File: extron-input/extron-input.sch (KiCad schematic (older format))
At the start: 16 parts, among them J1 SCART-F, J10 Conn_01x01, J11 Conn_01x01, J2 RED, J3 GREEN, J4 BLUE, J5 SYNC, J6 PHOENIX, J7 SENSE, J8 Conn_01x01, J9 Conn_01x01, SW1 SW_DPDT_x2, U1 LM1881

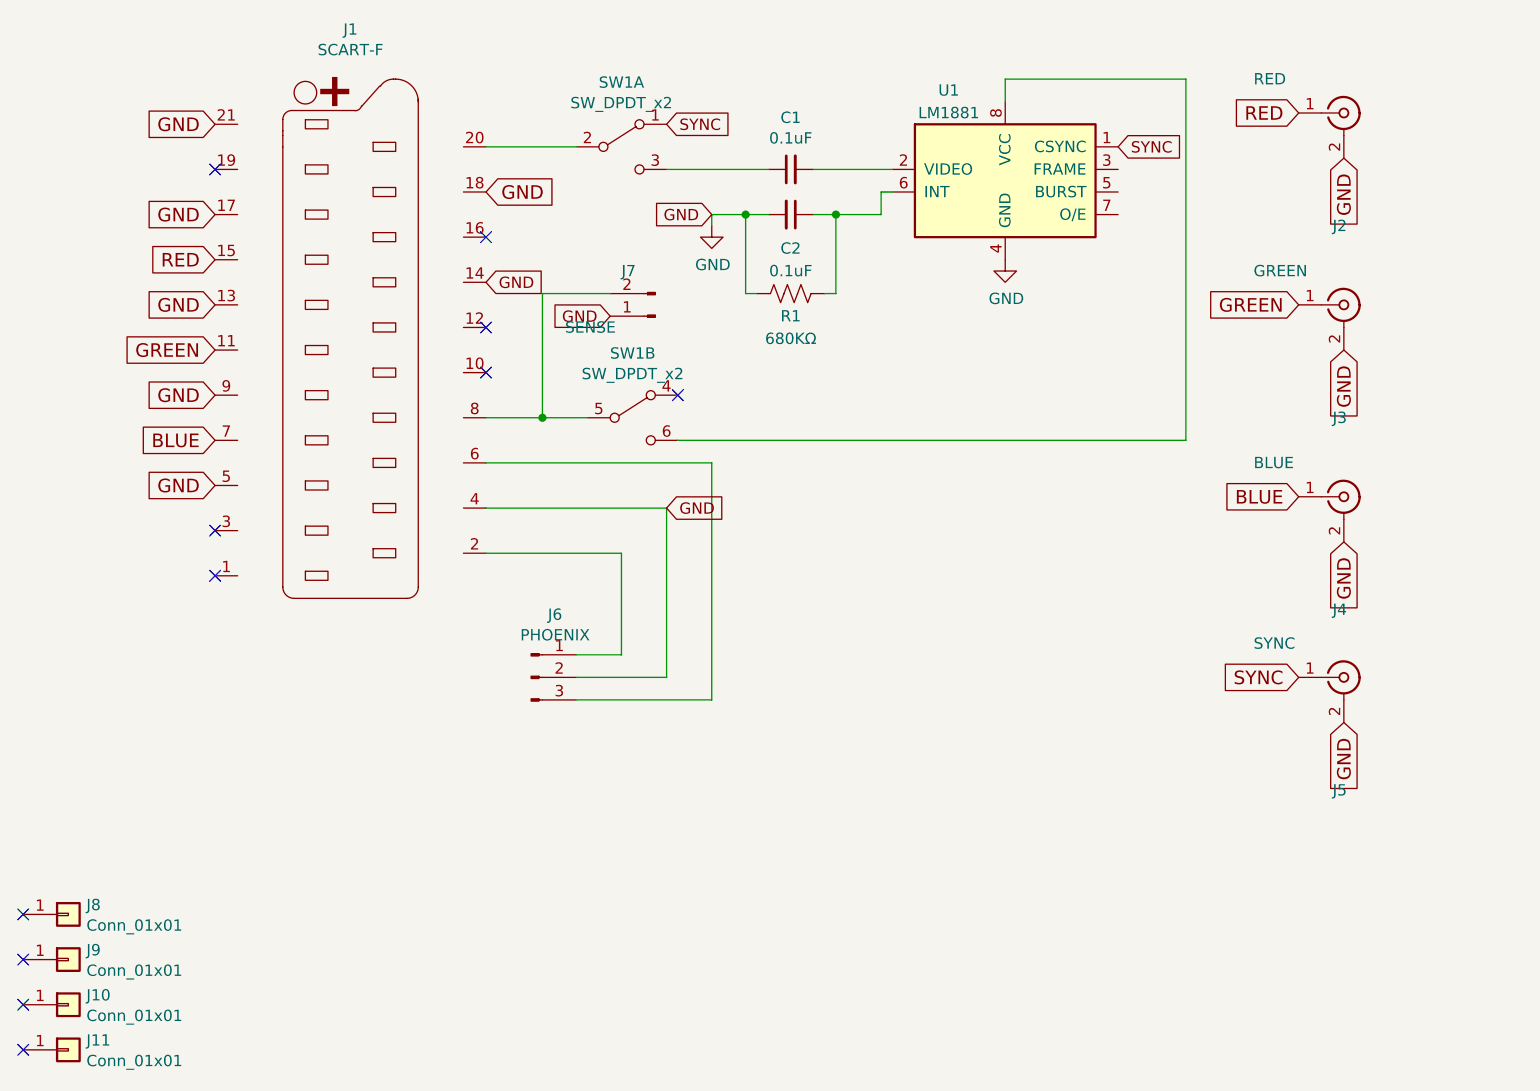
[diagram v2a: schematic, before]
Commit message: Rev 2 input board (+ other small things)
BNC F -> RCA F for all outputs to extron
  The BNC is great, but expensive, and also impossible to close over an
  extron input when they are matrixed. The RCA female recepticles will
  all to use with RCA M -> BNC M adapters, which you can pre-load onto
  the extron BNC F inputs. This will allow cards to plug in
  individually, or all at once if you have a stack of cards held
  together with standoffs.

Sense circuit protection
  Added to the input board to create a 3v3 sense line to be used by an
  upcoming optional board. It also protects the SCART switch line from
  output from the optional board, just in case. This entire circuit is
  totally optional. If you're not using the upcoming sense board, then
  you can leave this unpopulated.

New footprints for 2 different types of RCA
  There's an available RCA female PCB mount footprint that I found here:
  http://smisioto.no-ip.org/elettronica/kicad/kicad-en.htm . I also
  created my own footprint for the only RCA part on lcsc.com, because if
  that one works, it's super inexpensive. You can use one or the other,
  I hope.

Gitignore added
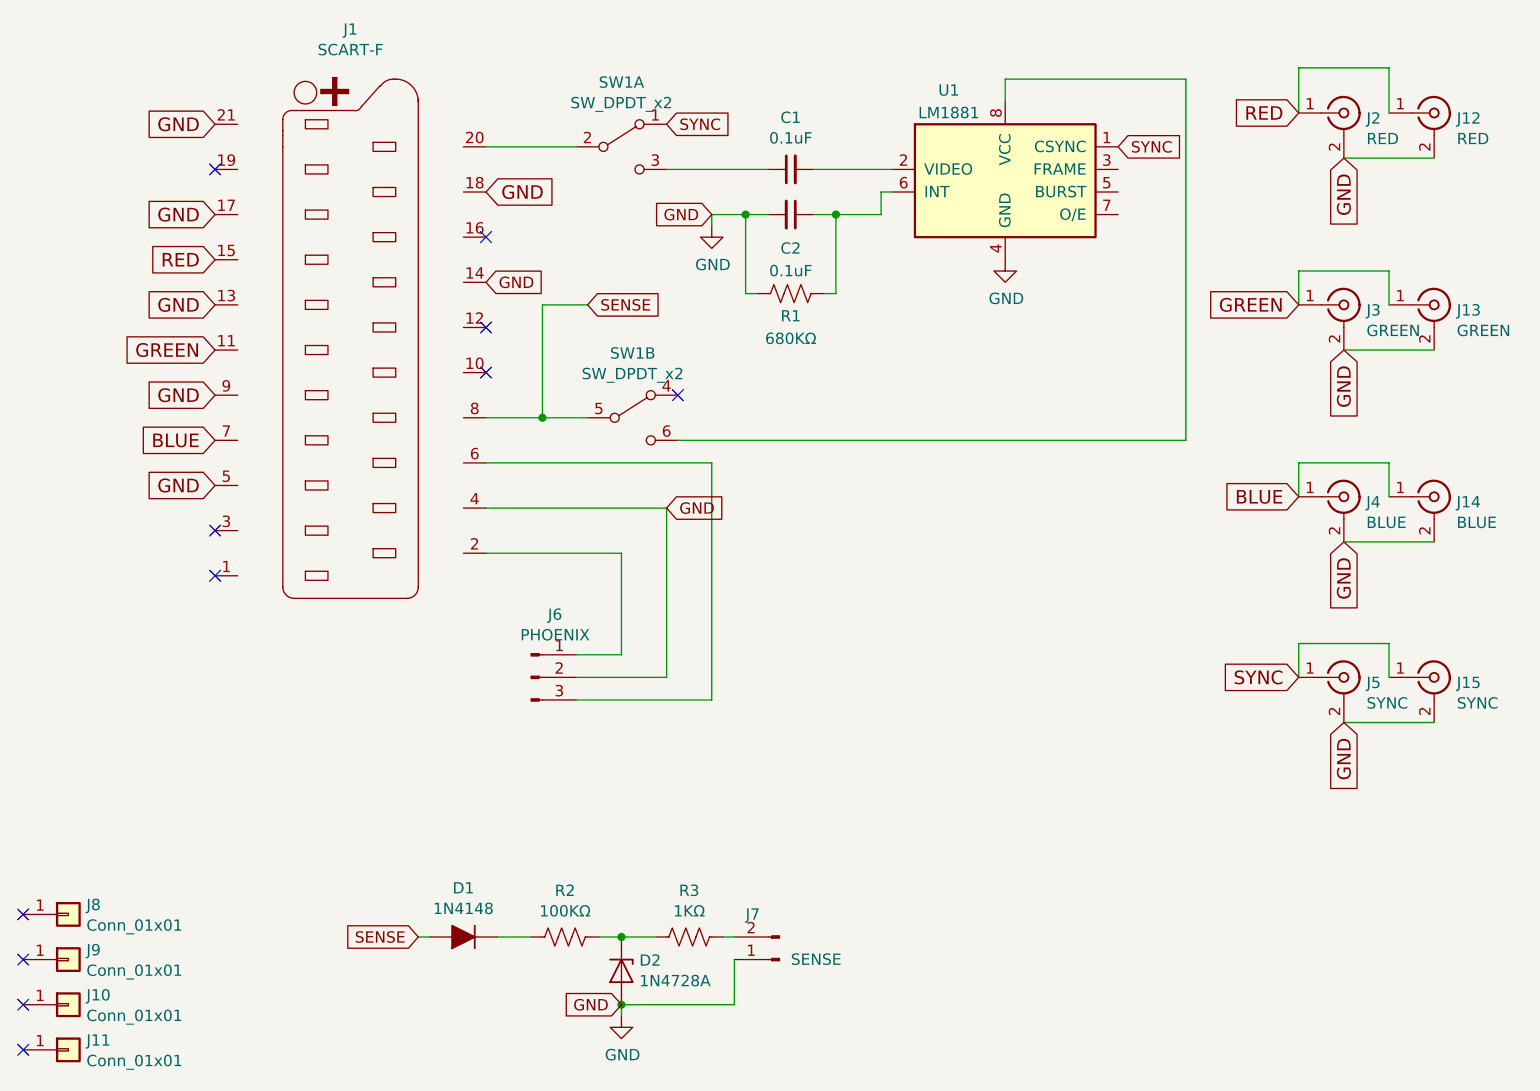
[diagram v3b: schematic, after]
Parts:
- added D1: 1N4148, Diode_THT:D_DO-35_SOD27_P2.54mm_Vertical_AnodeUp, symbol Device:D_ALT
- added D2: 1N4728A, Diode_THT:D_DO-35_SOD27_P2.54mm_Vertical_AnodeUp, symbol Device:D_Zener
- added J12: RED, extron-input:rca_black, symbol Connector:Conn_Coaxial
- added J13: GREEN, extron-input:rca_black, symbol Connector:Conn_Coaxial
- added J14: BLUE, extron-input:rca_black, symbol Connector:Conn_Coaxial
- added J15: SYNC, extron-input:rca_black, symbol Connector:Conn_Coaxial
- added R2: 100KΩ, Resistor_THT:R_Axial_DIN0204_L3.6mm_D1.6mm_P1.90mm_Vertical, symbol Device:R_US
- added R3: 1KΩ, Resistor_THT:R_Axial_DIN0204_L3.6mm_D1.6mm_P1.90mm_Vertical, symbol Device:R_US
- J2, J3, J4, J5: footprint extron-input:BNC_90 -> extron-input:rca_boom
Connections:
- net BLUE: now also J14.1 (In)
- net GND: now also D2.2 (A), J12.2 (Ext), J13.2 (Ext), J14.2 (Ext), J15.2 (Ext)
- net GREEN: now also J13.1 (In)
- net RED: now also J12.1 (In)
- net SYNC: now also J15.1 (In)
- net SENSE: now reaches J1.8 (P8), SW1.5 (B)
- net SENSE: now also D1.2 (A); no longer J7.2 (Pin_2)
- new net: J7.2 (Pin_2), R3.1
- new net: D1.1 (K), R2.2
- new net: D2.1 (K), R2.1, R3.2
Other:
- moved on the sheet: J7
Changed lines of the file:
@@
 Text GLabel 8050 2050 0    60   Input ~ 0
 RED
-$Comp
-L Connector:Conn_Coaxial J2
-U 1 1 5C651C5B
-P 8250 2050
-F 0 "J2" H 8200 1550 50  0000 L CNN
-F 1 "RED" H 7850 2200 50  0000 L CNN
-F 2 "extron-input:BNC_90" H 8250 2050 50  0001 C CNN
-F 3 " ~" H 8250 2050 50  0001 C CNN
-	1    8250 2050
-	1    0    0    -1
-$EndComp
-$Comp
-L Connector:Conn_Coaxial J3
-U 1 1 5C651D00
-P 8250 2900
-F 0 "J3" H 8200 2400 50  0000 L CNN
-F 1 "GREEN" H 7850 3050 50  0000 L CNN
-F 2 "extron-input:BNC_90" H 8250 2900 50  0001 C CNN
-F 3 " ~" H 8250 2900 50  0001 C CNN
-	1    8250 2900
-	1    0    0    -1
-$EndComp
-$Comp
-L Connector:Conn_Coaxial J4
-U 1 1 5C651DB2
-P 8250 3750
-F 0 "J4" H 8200 3250 50  0000 L CNN
-F 1 "BLUE" H 7850 3900 50  0000 L CNN
-F 2 "extron-input:BNC_90" H 8250 3750 50  0001 C CNN
-F 3 " ~" H 8250 3750 50  0001 C CNN
-	1    8250 3750
-	1    0    0    -1
-$EndComp
-$Comp
-L Connector:Conn_Coaxial J5
-U 1 1 5C651E83
-P 8250 4550
-F 0 "J5" H 8200 4050 50  0000 L CNN
-F 1 "SYNC" H 7850 4700 50  0000 L CNN
-F 2 "extron-input:BNC_90" H 8250 4550 50  0001 C CNN
-F 3 " ~" H 8250 4550 50  0001 C CNN
-	1    8250 4550
-	1    0    0    -1
-$EndComp
 Text GLabel 8250 3100 3    60   Input ~ 0
 GND
@@
 L Connector:Conn_01x02_Male J7
 U 1 1 5C74DAFA
-P 5200 2950
-F 0 "J7" H 5350 2750 50  0000 R CNN
-F 1 "SENSE" H 5600 3000 50  0000 R CNN
-F 2 "Connector_JST:JST_XH_S02B-XH-A_1x02_P2.50mm_Horizontal" H 5200 2950 50  0001 C CNN
-F 3 "~" H 5200 2950 50  0001 C CNN
-	1    5200 2950
+P 5750 5800
+F 0 "J7" H 5900 5600 50  0000 R CNN
+F 1 "SENSE" H 5700 5800 50  0000 R CNN
+F 2 "Connector_JST:JST_XH_S02B-XH-A_1x02_P2.50mm_Horizontal" H 5750 5800 50  0001 C CNN
+F 3 "~" H 5750 5800 50  0001 C CNN
+	1    5750 5800
 	-1   0    0    1
 $EndComp
@@
 Wire Wire Line
 	4700 3400 4900 3400
-Text GLabel 5000 2950 0    50   Input ~ 0
+Text GLabel 5050 6000 0    50   Input ~ 0
 GND
 Wire Wire Line
@@
 	4850 4650 5450 4650
 Wire Wire Line
-	4700 2850 5000 2850
-Wire Wire Line
-	4700 2850 4700 3400
+	4700 2900 4900 2900
+Wire Wire Line
+	4700 2900 4700 3400
+Text GLabel 4900 2900 2    50   Input ~ 0
+SENSE
+Wire Wire Line
+	5550 5700 5500 5700
+$Comp
+L Device:D_ALT D1
+U 1 1 5C84733C
+P 4350 5700
+F 0 "D1" H 4350 5484 50  0000 C CNN
+F 1 "1N4148" H 4350 5575 50  0000 C CNN
+F 2 "Diode_THT:D_DO-35_SOD27_P2.54mm_Vertical_AnodeUp" H 4350 5700 50  0001 C CNN
+F 3 "~" H 4350 5700 50  0001 C CNN
+	1    4350 5700
+	-1   0    0    1
+$EndComp
+$Comp
+L Device:R_US R2
+U 1 1 5C847B71
+P 4800 5700
+F 0 "R2" V 4595 5700 50  0000 C CNN
+F 1 "100KΩ" V 4686 5700 50  0000 C CNN
+F 2 "Resistor_THT:R_Axial_DIN0204_L3.6mm_D1.6mm_P1.90mm_Vertical" V 4840 5690 50  0001 C CNN
+F 3 "~" H 4800 5700 50  0001 C CNN
+	1    4800 5700
+	0    1    1    0
+$EndComp
+$Comp
+L Device:D_Zener D2
+U 1 1 5C847C9D
+P 5050 5850
+F 0 "D2" V 5004 5929 50  0000 L CNN
+F 1 "1N4728A" V 5095 5929 50  0000 L CNN
+F 2 "Diode_THT:D_DO-35_SOD27_P2.54mm_Vertical_AnodeUp" H 5050 5850 50  0001 C CNN
+F 3 "~" H 5050 5850 50  0001 C CNN
+	1    5050 5850
+	0    1    1    0
+$EndComp
+Wire Wire Line
+	4950 5700 5050 5700
+Connection ~ 5050 5700
+Text GLabel 4150 5700 0    50   Input ~ 0
+SENSE
+$Comp
+L power:GND #PWR0103
+U 1 1 5C849937
+P 5050 6050
+F 0 "#PWR0103" H 5050 5800 50  0001 C CNN
+F 1 "GND" H 5055 5877 50  0000 C CNN
+F 2 "" H 5050 6050 50  0001 C CNN
+F 3 "" H 5050 6050 50  0001 C CNN
+	1    5050 6050
+	1    0    0    -1
+$EndComp
+Wire Wire Line
+	5550 5800 5550 6000
+Wire Wire Line
+	5550 6000 5050 6000
+Connection ~ 5050 6000
+Wire Wire Line
+	5050 6000 5050 6050
+$Comp
+L Device:R_US R3
+U 1 1 5C84AF3E
+P 5350 5700
+F 0 "R3" V 5145 5700 50  0000 C CNN
+F 1 "1KΩ" V 5236 5700 50  0000 C CNN
+F 2 "Resistor_THT:R_Axial_DIN0204_L3.6mm_D1.6mm_P1.90mm_Vertical" V 5390 5690 50  0001 C CNN
+F 3 "~" H 5350 5700 50  0001 C CNN
+	1    5350 5700
+	0    1    1    0
+$EndComp
+Wire Wire Line
+	5200 5700 5050 5700
+Wire Wire Line
+	4150 5700 4200 5700
+Wire Wire Line
+	4500 5700 4650 5700
+$Comp
+L Connector:Conn_Coaxial J12
+U 1 1 5C84CB4A
+P 8650 2050
+F 0 "J12" H 8750 2026 50  0000 L CNN
+F 1 "RED" H 8750 1935 50  0000 L CNN
+F 2 "extron-input:rca_black" H 8650 2050 50  0001 C CNN
+F 3 " ~" H 8650 2050 50  0001 C CNN
+	1    8650 2050
+	1    0    0    -1
+$EndComp
+Wire Wire Line
+	8050 1850 8050 2050
+Wire Wire Line
+	8250 2250 8650 2250
+Wire Wire Line
+	8050 1850 8450 1850
+Wire Wire Line
+	8450 1850 8450 2050
+$Comp
+L Connector:Conn_Coaxial J13
+U 1 1 5C84FDFD
+P 8650 2900
+F 0 "J13" H 8750 2876 50  0000 L CNN
+F 1 "GREEN" H 8750 2785 50  0000 L CNN
+F 2 "extron-input:rca_black" H 8650 2900 50  0001 C CNN
+F 3 " ~" H 8650 2900 50  0001 C CNN
+	1    8650 2900
+	1    0    0    -1
+$EndComp
+$Comp
+L Connector:Conn_Coaxial J14
+U 1 1 5C84FE72
+P 8650 3750
+F 0 "J14" H 8749 3726 50  0000 L CNN
+F 1 "BLUE" H 8749 3635 50  0000 L CNN
+F 2 "extron-input:rca_black" H 8650 3750 50  0001 C CNN
+F 3 " ~" H 8650 3750 50  0001 C CNN
+	1    8650 3750
+	1    0    0    -1
+$EndComp
+$Comp
+L Connector:Conn_Coaxial J15
+U 1 1 5C84FF62
+P 8650 4550
+F 0 "J15" H 8750 4526 50  0000 L CNN
+F 1 "SYNC" H 8750 4435 50  0000 L CNN
+F 2 "extron-input:rca_black" H 8650 4550 50  0001 C CNN
+F 3 " ~" H 8650 4550 50  0001 C CNN
+	1    8650 4550
+	1    0    0    -1
+$EndComp
+Wire Wire Line
+	8650 4750 8250 4750
+Wire Wire Line
+	8450 4550 8450 4400
+Wire Wire Line
+	8450 4400 8050 4400
+Wire Wire Line
+	8050 4400 8050 4550
+Wire Wire Line
+	8650 3950 8250 3950
+Wire Wire Line
+	8050 3750 8050 3600
+Wire Wire Line
+	8050 3600 8450 3600
+Wire Wire Line
+	8450 3600 8450 3750
+Wire Wire Line
+	8250 3100 8650 3100
+Wire Wire Line
+	8050 2900 8050 2750
+Wire Wire Line
+	8050 2750 8450 2750
+Wire Wire Line
+	8450 2750 8450 2900
+$Comp
+L Connector:Conn_Coaxial J2
+U 1 1 5C8498CA
+P 8250 2050
+F 0 "J2" H 8350 2026 50  0000 L CNN
+F 1 "RED" H 8350 1935 50  0000 L CNN
+F 2 "extron-input:rca_boom" H 8250 2050 50  0001 C CNN
+F 3 " ~" H 8250 2050 50  0001 C CNN
+	1    8250 2050
+	1    0    0    -1
+$EndComp
+$Comp
+L Connector:Conn_Coaxial J3
+U 1 1 5C849928
+P 8250 2900
+F 0 "J3" H 8350 2876 50  0000 L CNN
+F 1 "GREEN" H 8350 2785 50  0000 L CNN
+F 2 "extron-input:rca_boom" H 8250 2900 50  0001 C CNN
+F 3 " ~" H 8250 2900 50  0001 C CNN
+	1    8250 2900
+	1    0    0    -1
+$EndComp
+$Comp
+L Connector:Conn_Coaxial J4
+U 1 1 5C84997A
+P 8250 3750
+F 0 "J4" H 8349 3726 50  0000 L CNN
+F 1 "BLUE" H 8349 3635 50  0000 L CNN
+F 2 "extron-input:rca_boom" H 8250 3750 50  0001 C CNN
+F 3 " ~" H 8250 3750 50  0001 C CNN
+	1    8250 3750
+	1    0    0    -1
+$EndComp
+$Comp
+L Connector:Conn_Coaxial J5
+U 1 1 5C8499F8
+P 8250 4550
+F 0 "J5" H 8350 4526 50  0000 L CNN
+F 1 "SYNC" H 8350 4435 50  0000 L CNN
+F 2 "extron-input:rca_boom" H 8250 4550 50  0001 C CNN
+F 3 " ~" H 8250 4550 50  0001 C CNN
+	1    8250 4550
+	1    0    0    -1
+$EndComp
 $EndSCHEMATC

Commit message: Added vendor/link to all schematic parts
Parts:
- C1, C2: Vendor (none) -> https://lcsc.com/product-detail/Multilayer-Ceramic-Capacito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
- D1: Vendor (none) -> https://lcsc.com/product-detail/Switching-Diode_1N4148_C145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
- D2: Vendor (none) -> https://lcsc.com/product-detail/Zener-Diodes_ON-Semicon_1N4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
- J1: Vendor (none) -> https://console5.com/store/female-scart-jp21-through-hole-p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
- J12: Vendor (none) -> https://www.arrow.com/en/products/rcj-042/cui-inc
- J13: Vendor (none) -> https://www.arrow.com/en/products/rcj-046/cui-inc
- J14: Vendor (none) -> https://www.arrow.com/en/products/rcj-045/cui-inc
- J15: Vendor (none) -> https://www.arrow.com/en/products/rcj-044/cui-inc
- J2, J3, J4, J5: Vendor (none) -> https://lcsc.com/product-detail/AV-Connectors_AV-5_C18080.h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
- J6: Vendor (none) -> https://lcsc.com/product-detail/XH-Connectors_JST_S3B-XH-A-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
- J7: Vendor (none) -> https://lcsc.com/product-detail/XH-Connectors_JST_S2B-XH-A-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
- R1: Vendor (none) -> https://lcsc.com/product-detail/Others_FlyWin-CR1-8W-5-680K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
- R2: Vendor (none) -> https://lcsc.com/product-detail/Carbon-Film-Resistors_100KR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
- R3: Vendor (none) -> https://lcsc.com/product-detail/Carbon-Film-Resistors_1KR-1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
- SW1: Vendor (none) -> https://lcsc.com/product-detail/Toggle-Switches_C-K_JS20201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
- U1: Vendor (none) -> https://www.ti.com/store/ti/en/p/product/?p=LM1881N/NOPB&HQ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
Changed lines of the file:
@@
 F 2 "extron-input:SCART_F_RA" H 3850 3150 50  0001 C CNN
 F 3 " ~" H 3850 3150 50  0001 C CNN
+F 4 "https://console5.com/store/female-scart-jp21-through-hole-pcb-mount-21-pin-connector-right-angle.html" H 3850 3100 50  0001 C CNN "Vendor"
 	1    3850 3100
 	1    0    0    -1
@@
 F 2 "Connector_JST:JST_XH_S03B-XH-A_1x03_P2.50mm_Horizontal" H 4650 4550 50  0001 C CNN
 F 3 "~" H 4650 4550 50  0001 C CNN
+F 4 "https://lcsc.com/product-detail/XH-Connectors_JST_S3B-XH-A-LF-SN_XHsocket-1-3P-Curved-needle-pitch2-5mm_C157928.html" H 4650 4550 50  0001 C CNN "Vendor"
 	1    4650 4550
 	1    0    0    -1
@@
 F 2 "Connector_JST:JST_XH_S02B-XH-A_1x02_P2.50mm_Horizontal" H 5750 5800 50  0001 C CNN
 F 3 "~" H 5750 5800 50  0001 C CNN
+F 4 "https://lcsc.com/product-detail/XH-Connectors_JST_S2B-XH-A-LF-SN_XHsocket-1-2P-Curved-needle-pitch2-5mm_C157931.html" H 5750 5800 50  0001 C CNN "Vendor"
 	1    5750 5800
 	-1   0    0    1
@@
 F 2 "Package_DIP:DIP-8_W7.62mm" H 6750 2400 50  0001 C CNN
 F 3 "" H 6750 2400 50  0001 C CNN
+F 4 "https://www.ti.com/store/ti/en/p/product/?p=LM1881N/NOPB&HQS=corp-tistore-null-storeinv-invf-store-octopart-wwe" H 6750 2400 50  0001 C CNN "Vendor"
 	1    6750 2400
 	1    0    0    -1
@@
 F 2 "Resistor_THT:R_Axial_DIN0204_L3.6mm_D1.6mm_P1.90mm_Vertical" V 5840 2840 50  0001 C CNN
 F 3 "~" H 5800 2850 50  0001 C CNN
+F 4 "https://lcsc.com/product-detail/Others_FlyWin-CR1-8W-5-680K-OTB5_C337028.html" V 5800 2850 50  0001 C CNN "Vendor"
 	1    5800 2850
 	0    -1   -1   0
@@
 F 2 "Capacitor_THT:C_Disc_D3.0mm_W1.6mm_P2.50mm" H 5800 2500 50  0001 C CNN
 F 3 "~" H 5800 2500 50  0001 C CNN
+F 4 "https://lcsc.com/product-detail/Multilayer-Ceramic-Capacitors-MLCC-Leaded_100nF-104-20-100V_C154503.html" V 5800 2500 50  0001 C CNN "Vendor"
 	1    5800 2500
 	0    1    1    0
@@
 F 2 "Capacitor_THT:C_Disc_D3.0mm_W1.6mm_P2.50mm" H 5800 2300 50  0001 C CNN
 F 3 "~" H 5800 2300 50  0001 C CNN
+F 4 "https://lcsc.com/product-detail/Multilayer-Ceramic-Capacitors-MLCC-Leaded_100nF-104-20-100V_C154503.html" V 5800 2300 50  0001 C CNN "Vendor"
 	1    5800 2300
 	0    -1   -1   0
@@
 F 2 "Button_Switch_THT:SW_CuK_JS202011AQN_DPDT_Angled" H 5100 3400 50  0001 C CNN
 F 3 "" H 5100 3400 50  0001 C CNN
+F 4 "https://lcsc.com/product-detail/Toggle-Switches_C-K_JS202011AQN_C-K-JS202011AQN_C221662.html" H 5100 3400 50  0001 C CNN "Vendor"
 	2    5100 3400
 	1    0    0    -1
@@
 F 2 "Diode_THT:D_DO-35_SOD27_P2.54mm_Vertical_AnodeUp" H 4350 5700 50  0001 C CNN
 F 3 "~" H 4350 5700 50  0001 C CNN
+F 4 "https://lcsc.com/product-detail/Switching-Diode_1N4148_C14516.html" H 4350 5700 50  0001 C CNN "Vendor"
 	1    4350 5700
 	-1   0    0    1
@@
 F 2 "Resistor_THT:R_Axial_DIN0204_L3.6mm_D1.6mm_P1.90mm_Vertical" V 4840 5690 50  0001 C CNN
 F 3 "~" H 4800 5700 50  0001 C CNN
+F 4 "https://lcsc.com/product-detail/Carbon-Film-Resistors_100KR-104-5_C120103.html" V 4800 5700 50  0001 C CNN "Vendor"
 	1    4800 5700
 	0    1    1    0
@@
 F 2 "Diode_THT:D_DO-35_SOD27_P2.54mm_Vertical_AnodeUp" H 5050 5850 50  0001 C CNN
 F 3 "~" H 5050 5850 50  0001 C CNN
+F 4 "https://lcsc.com/product-detail/Zener-Diodes_ON-Semicon_1N4728A_ON-Semicon-ON-1N4728A_C140852.html" V 5050 5850 50  0001 C CNN "Vendor"
 	1    5050 5850
 	0    1    1    0
@@
 F 2 "Resistor_THT:R_Axial_DIN0204_L3.6mm_D1.6mm_P1.90mm_Vertical" V 5390 5690 50  0001 C CNN
 F 3 "~" H 5350 5700 50  0001 C CNN
+F 4 "https://lcsc.com/product-detail/Carbon-Film-Resistors_1KR-102-5_C120055.html" V 5350 5700 50  0001 C CNN "Vendor"
 	1    5350 5700
 	0    1    1    0
@@
 F 2 "extron-input:rca_black" H 8650 2050 50  0001 C CNN
 F 3 " ~" H 8650 2050 50  0001 C CNN
+F 4 "https://www.arrow.com/en/products/rcj-042/cui-inc" H 8650 2050 50  0001 C CNN "Vendor"
 	1    8650 2050
 	1    0    0    -1
@@
 F 2 "extron-input:rca_black" H 8650 2900 50  0001 C CNN
 F 3 " ~" H 8650 2900 50  0001 C CNN
+F 4 "https://www.arrow.com/en/products/rcj-046/cui-inc" H 8650 2900 50  0001 C CNN "Vendor"
 	1    8650 2900
 	1    0    0    -1
@@
 F 2 "extron-input:rca_black" H 8650 3750 50  0001 C CNN
 F 3 " ~" H 8650 3750 50  0001 C CNN
+F 4 "https://www.arrow.com/en/products/rcj-045/cui-inc" H 8650 3750 50  0001 C CNN "Vendor"
 	1    8650 3750
 	1    0    0    -1
@@
 F 2 "extron-input:rca_black" H 8650 4550 50  0001 C CNN
 F 3 " ~" H 8650 4550 50  0001 C CNN
+F 4 "https://www.arrow.com/en/products/rcj-044/cui-inc" H 8650 4550 50  0001 C CNN "Vendor"
 	1    8650 4550
 	1    0    0    -1
@@
 F 2 "extron-input:rca_boom" H 8250 2050 50  0001 C CNN
 F 3 " ~" H 8250 2050 50  0001 C CNN
+F 4 "https://lcsc.com/product-detail/AV-Connectors_AV-5_C18080.html" H 8250 2050 50  0001 C CNN "Vendor"
 	1    8250 2050
 	1    0    0    -1
@@
 F 2 "extron-input:rca_boom" H 8250 2900 50  0001 C CNN
 F 3 " ~" H 8250 2900 50  0001 C CNN
+F 4 "https://lcsc.com/product-detail/AV-Connectors_AV-5_C18080.html" H 8250 2900 50  0001 C CNN "Vendor"
 	1    8250 2900
 	1    0    0    -1
@@
 F 2 "extron-input:rca_boom" H 8250 3750 50  0001 C CNN
 F 3 " ~" H 8250 3750 50  0001 C CNN
+F 4 "https://lcsc.com/product-detail/AV-Connectors_AV-5_C18080.html" H 8250 3750 50  0001 C CNN "Vendor"
 	1    8250 3750
 	1    0    0    -1
@@
 F 2 "extron-input:rca_boom" H 8250 4550 50  0001 C CNN
 F 3 " ~" H 8250 4550 50  0001 C CNN
+F 4 "https://lcsc.com/product-detail/AV-Connectors_AV-5_C18080.html" H 8250 4550 50  0001 C CNN "Vendor"
 	1    8250 4550
 	1    0    0    -1
